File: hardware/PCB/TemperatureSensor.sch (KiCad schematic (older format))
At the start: 14 parts, among them J1 USB_B_Micro, U2 FT230XQ

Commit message: Complete Sensor schematic
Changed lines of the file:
@@
 F0 "Sensor" 50
 F1 "Sensor.sch" 50
+F2 "RST_SHT31" O R 2700 6600 50
+F3 "T_SHT31" O R 2700 6700 50
+F4 "RH_SHT31" O R 2700 6800 50
+F5 "SDA" O R 2700 7050 50
+F6 "SCL" O R 2700 7150 50
 $EndSheet
 $Sheet

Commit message: add 10k pull up
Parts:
- H1, H2, H3, H4: footprint MountingHole:MountingHole_2.2mm_M2_Pad_Via -> MountingHole:MountingHole_3.2mm_M3_Pad_Via
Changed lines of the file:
@@
 F 0 "H1" H 1000 2799 50  0000 L CNN
 F 1 "MountingHole_Pad" H 1000 2708 50  0000 L CNN
-F 2 "MountingHole:MountingHole_2.2mm_M2_Pad_Via" H 900 2750 50  0001 C CNN
+F 2 "MountingHole:MountingHole_3.2mm_M3_Pad_Via" H 900 2750 50  0001 C CNN
 F 3 "~" H 900 2750 50  0001 C CNN
 	1    900  2750
@@
 F 0 "H2" H 2000 2799 50  0000 L CNN
 F 1 "MountingHole_Pad" H 2000 2708 50  0000 L CNN
-F 2 "MountingHole:MountingHole_2.2mm_M2_Pad_Via" H 1900 2750 50  0001 C CNN
+F 2 "MountingHole:MountingHole_3.2mm_M3_Pad_Via" H 1900 2750 50  0001 C CNN
 F 3 "~" H 1900 2750 50  0001 C CNN
 	1    1900 2750
@@
 F 0 "H4" H 1800 3107 50  0000 R CNN
 F 1 "MountingHole_Pad" H 1800 3198 50  0000 R CNN
-F 2 "MountingHole:MountingHole_2.2mm_M2_Pad_Via" H 1900 3150 50  0001 C CNN
+F 2 "MountingHole:MountingHole_3.2mm_M3_Pad_Via" H 1900 3150 50  0001 C CNN
 F 3 "~" H 1900 3150 50  0001 C CNN
 	1    1900 3150
@@
 F 0 "H3" H 800 3107 50  0000 R CNN
 F 1 "MountingHole_Pad" H 800 3198 50  0000 R CNN
-F 2 "MountingHole:MountingHole_2.2mm_M2_Pad_Via" H 900 3150 50  0001 C CNN
+F 2 "MountingHole:MountingHole_3.2mm_M3_Pad_Via" H 900 3150 50  0001 C CNN
 F 3 "~" H 900 3150 50  0001 C CNN
 	1    900  3150

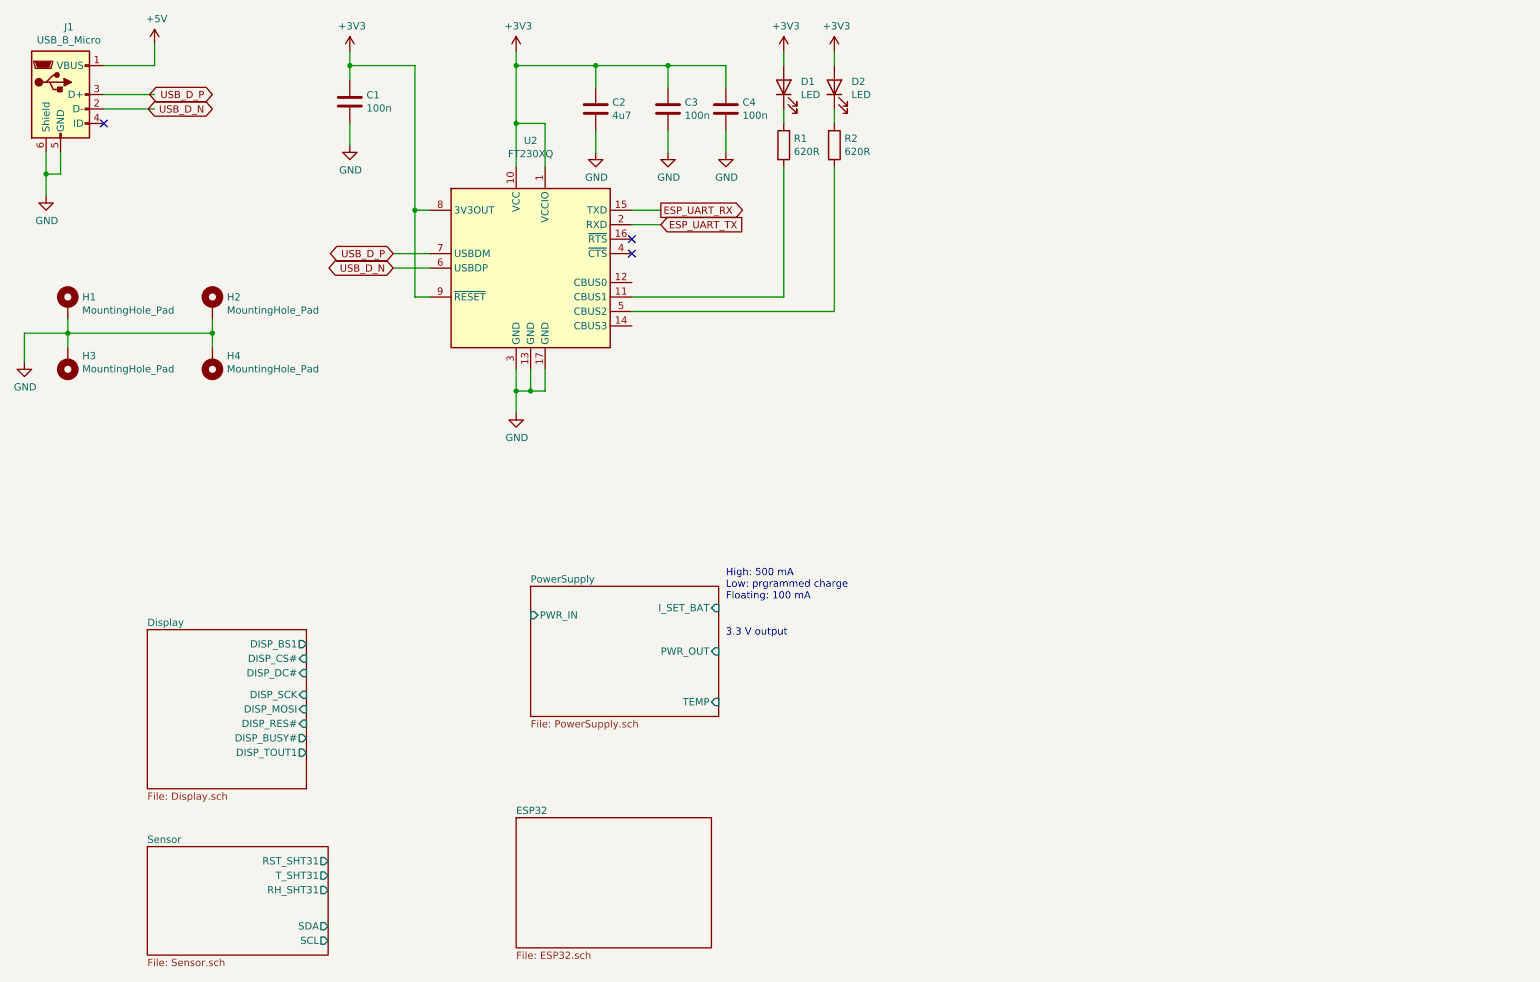
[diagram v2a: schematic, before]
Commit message: add mechannical and usb ftdi sheet
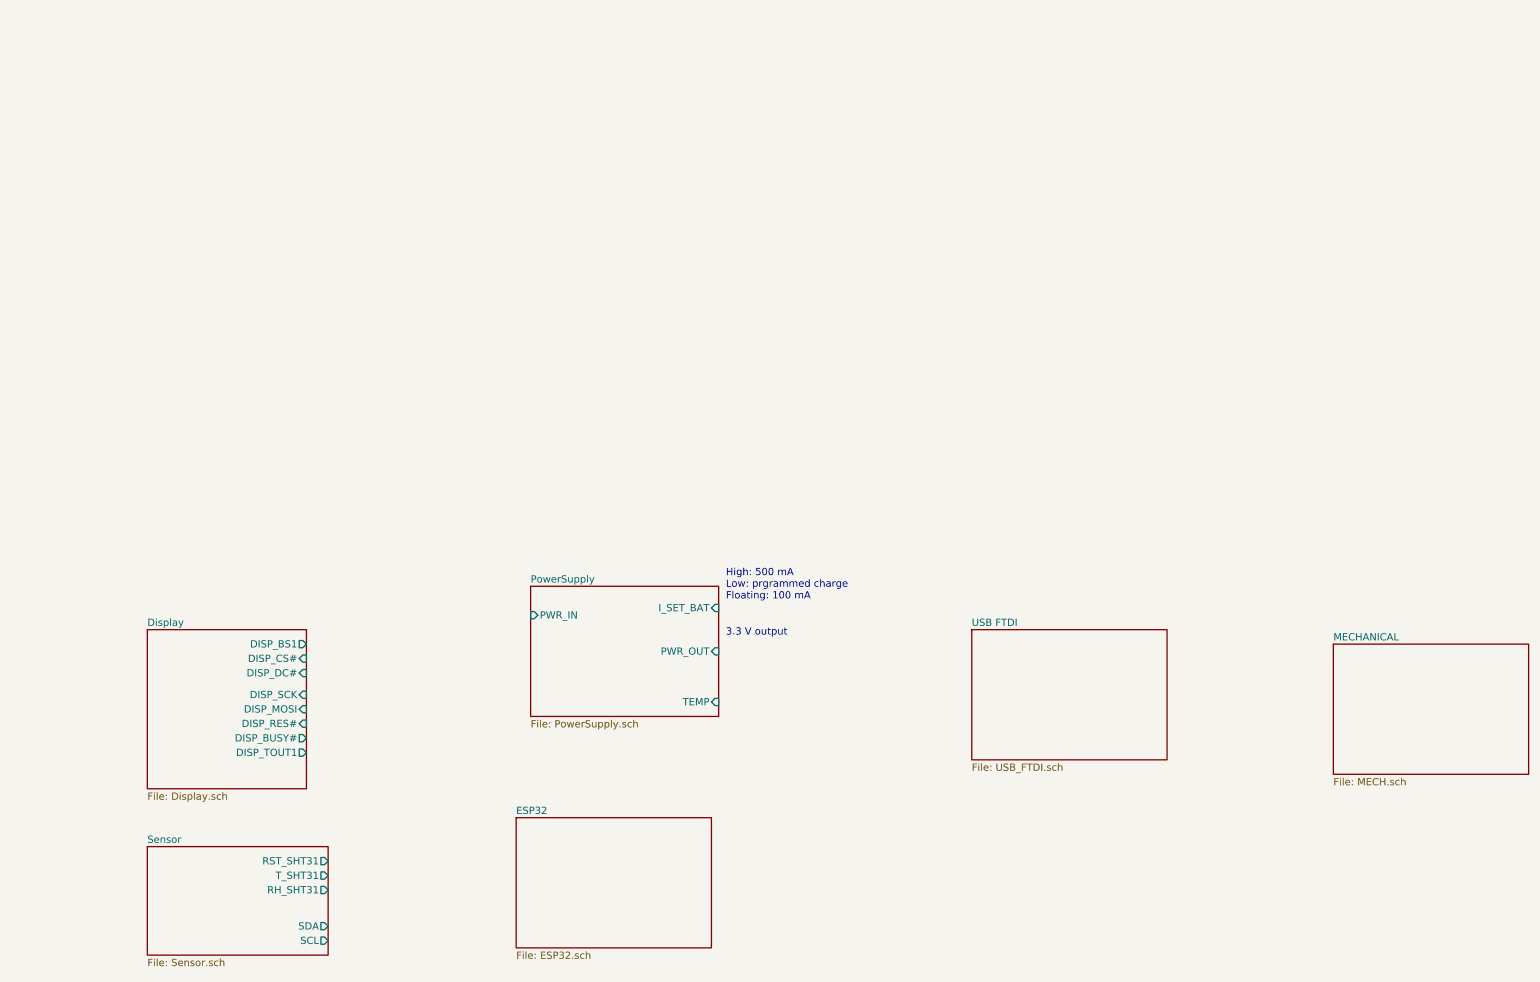
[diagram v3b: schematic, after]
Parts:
- removed C1, C3, C4: 100n, Capacitor_SMD:C_0603_1608Metric, symbol Device:C
- removed C2: 4u7, Capacitor_SMD:C_0603_1608Metric, symbol Device:C
- removed D1, D2: LED, LED_SMD:LED_0603_1608Metric, symbol Device:LED
- removed H1, H2, H3, H4: MountingHole_Pad, MountingHole:MountingHole_3.2mm_M3_Pad_Via, symbol Mechanical:MountingHole_Pad
- removed J1: USB_B_Micro, Connector_USB:USB_Micro-B_Amphenol_10118194_Horizontal, symbol Connector:USB_B_Micro
- removed R1, R2: 620R, Resistor_SMD:R_0603_1608Metric, symbol Device:R
- removed U2: FT230XQ, Package_DFN_QFN:QFN-16-1EP_4x4mm_P0.65mm_EP2.1x2.1mm, symbol Interface_USB:FT230XQ
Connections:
- net labels removed: +3V3, +5V, ESP_UART_RX, ESP_UART_TX, GND, USB_D_N, USB_D_P
- wire segments 55 -> 0
- no-connect marks 3 -> 0

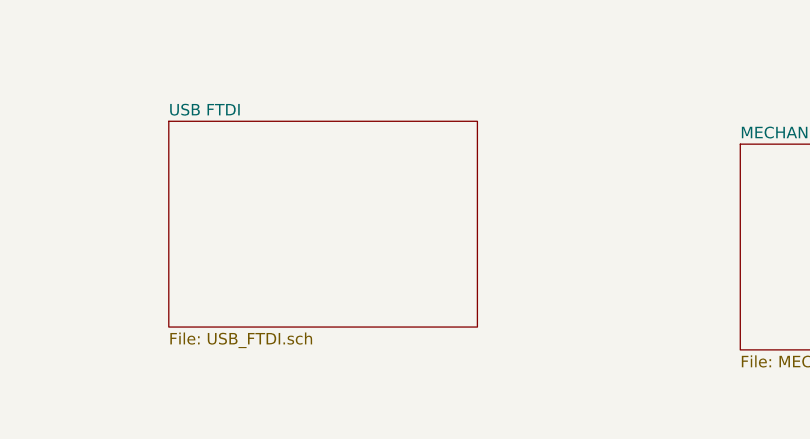
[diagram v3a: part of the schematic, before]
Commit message: add 32khz crystal for rtc
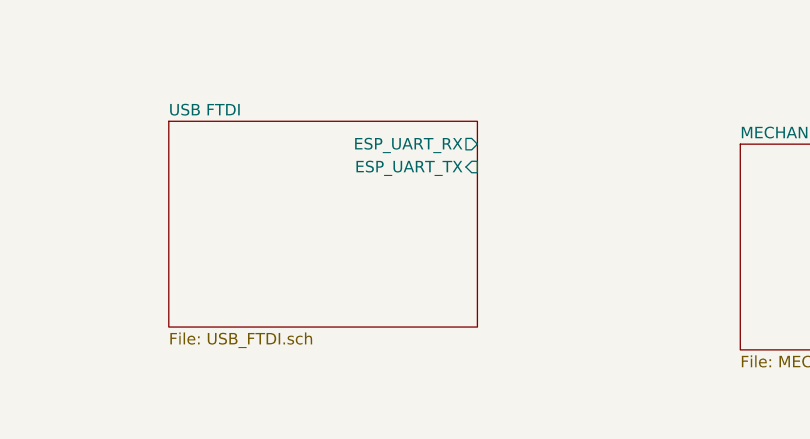
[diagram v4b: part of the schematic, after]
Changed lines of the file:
@@
 F0 "USB FTDI" 50
 F1 "USB_FTDI.sch" 50
+F2 "ESP_UART_RX" O R 8500 5100 50
+F3 "ESP_UART_TX" I R 8500 5200 50
 $EndSheet
 $EndSCHEMATC

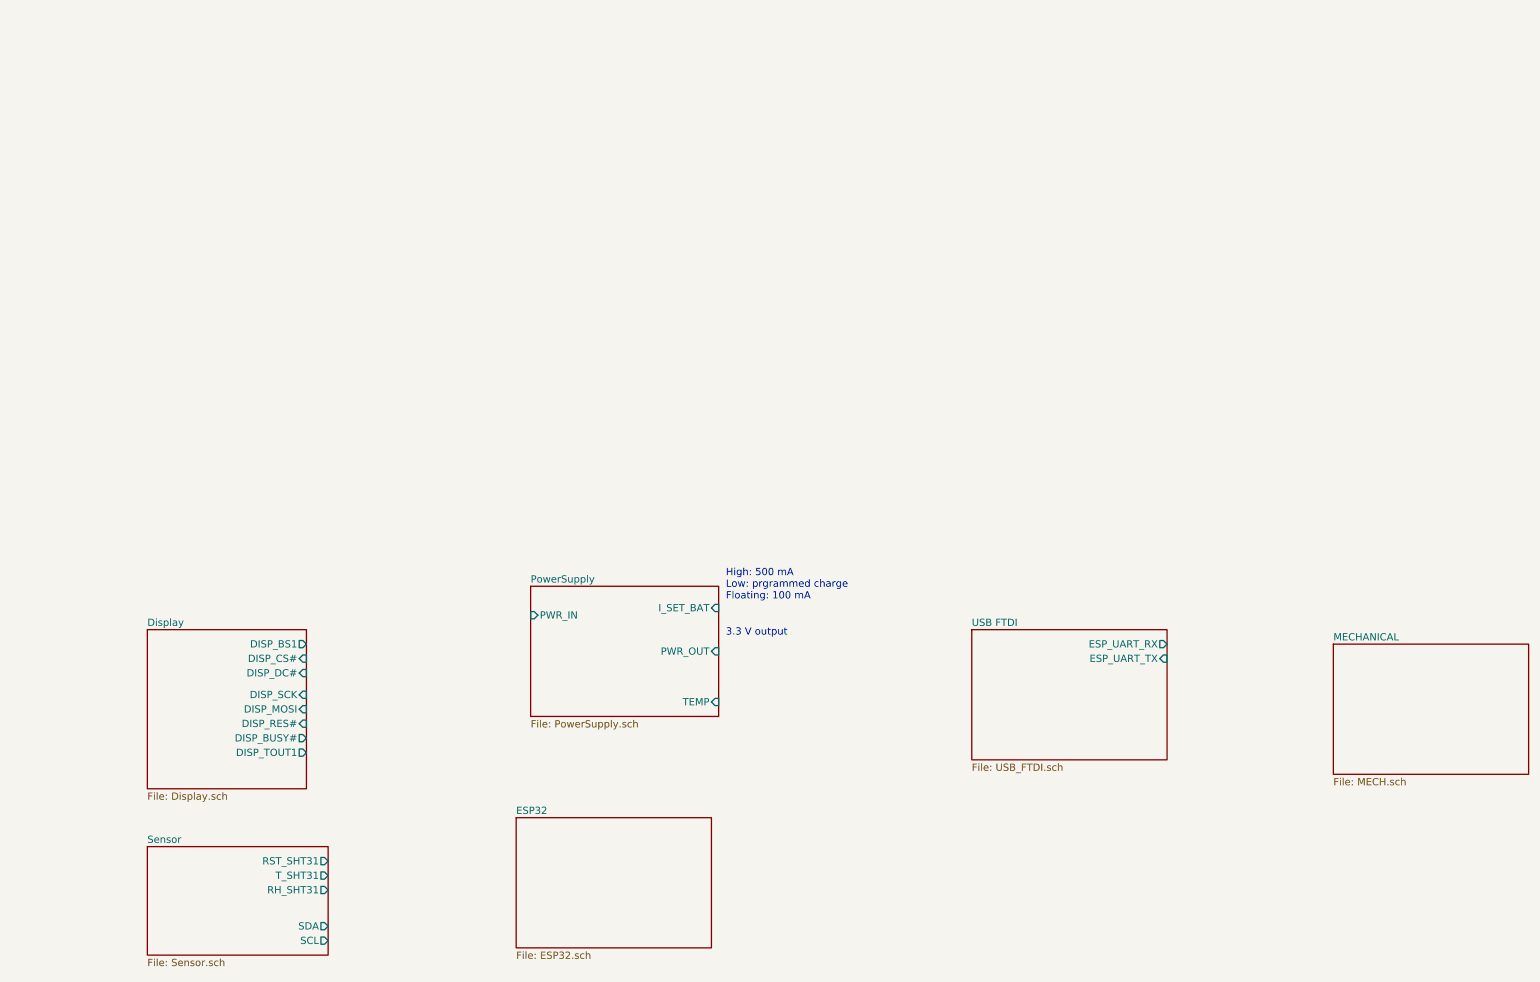
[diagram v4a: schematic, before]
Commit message: corrected power supply schematic
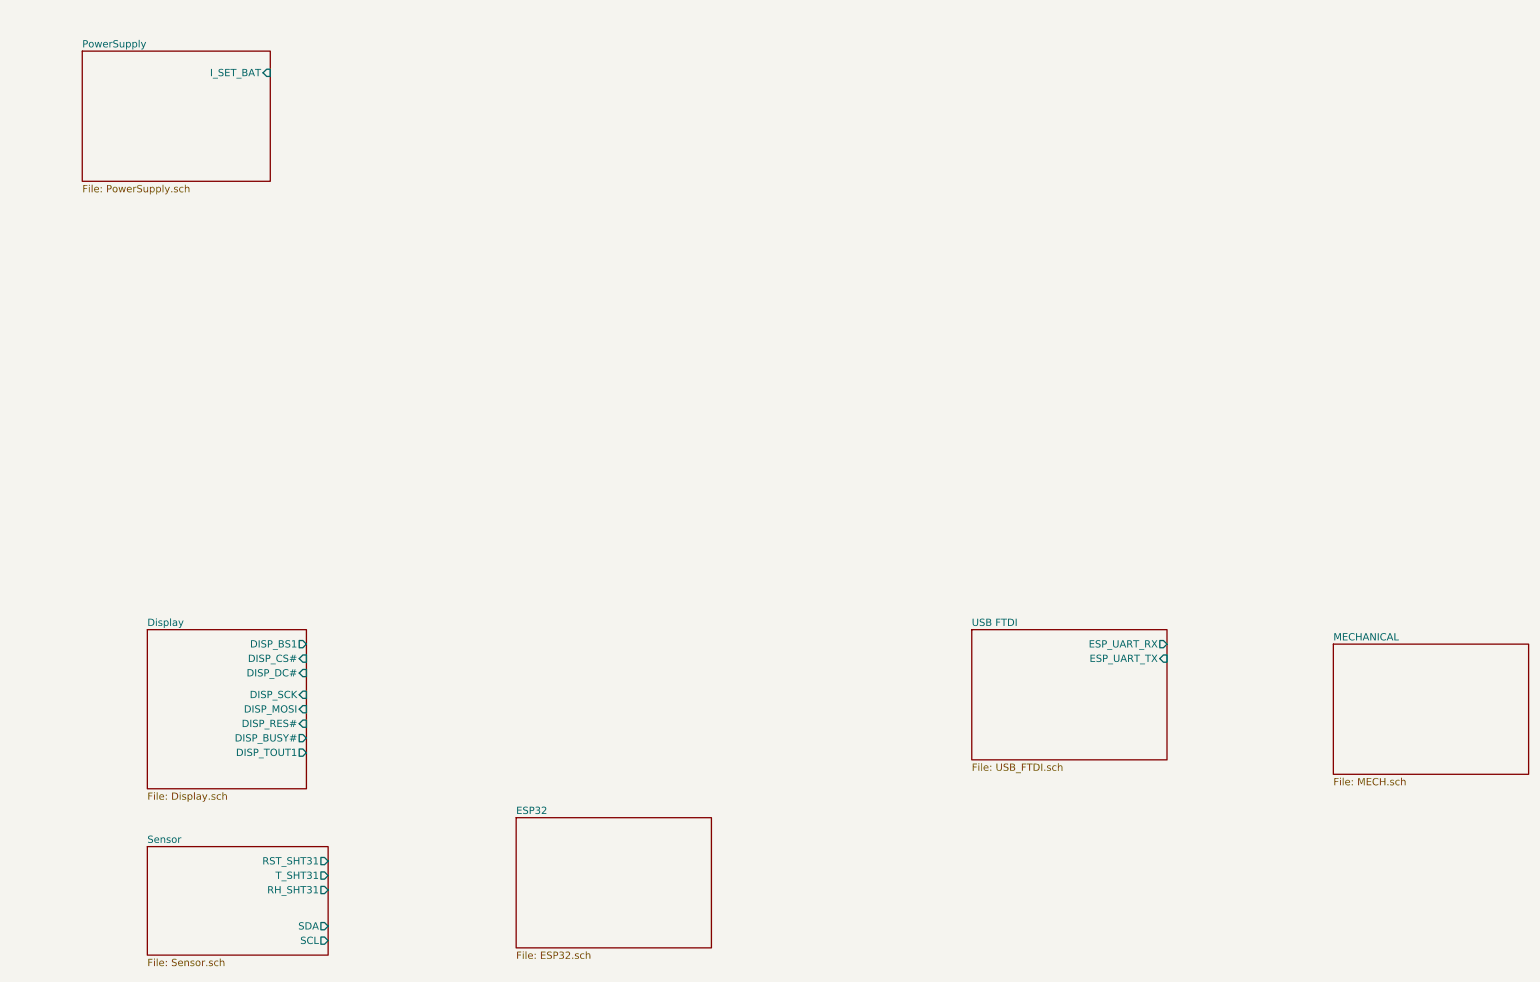
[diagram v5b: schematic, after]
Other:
- note removed: "3.3 V output"
- note removed: "High: 500 mA\nLow: prgrammed charge\nFloating: 100 mA"
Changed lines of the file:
@@
 $EndDescr
 $Sheet
-S 4100 4700 1300 900
+S 1000 1000 1300 900
 U 5FBFD530
 F0 "PowerSupply" 50
 F1 "PowerSupply.sch" 50
-F2 "PWR_IN" I L 4100 4900 50
-F3 "I_SET_BAT" I R 5400 4850 50
-F4 "TEMP" I R 5400 5500 50
-F5 "PWR_OUT" I R 5400 5150 50
+F2 "I_SET_BAT" I R 2300 1150 50
 $EndSheet
-Text Notes 5450 4800 0    50   ~ 0
-High: 500 mA\nLow: prgrammed charge\nFloating: 100 mA
-Text Notes 5450 5050 0    50   ~ 0
-3.3 V output
 $Sheet
 S 1450 5000 1100 1100

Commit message: add 40 MHz crystal
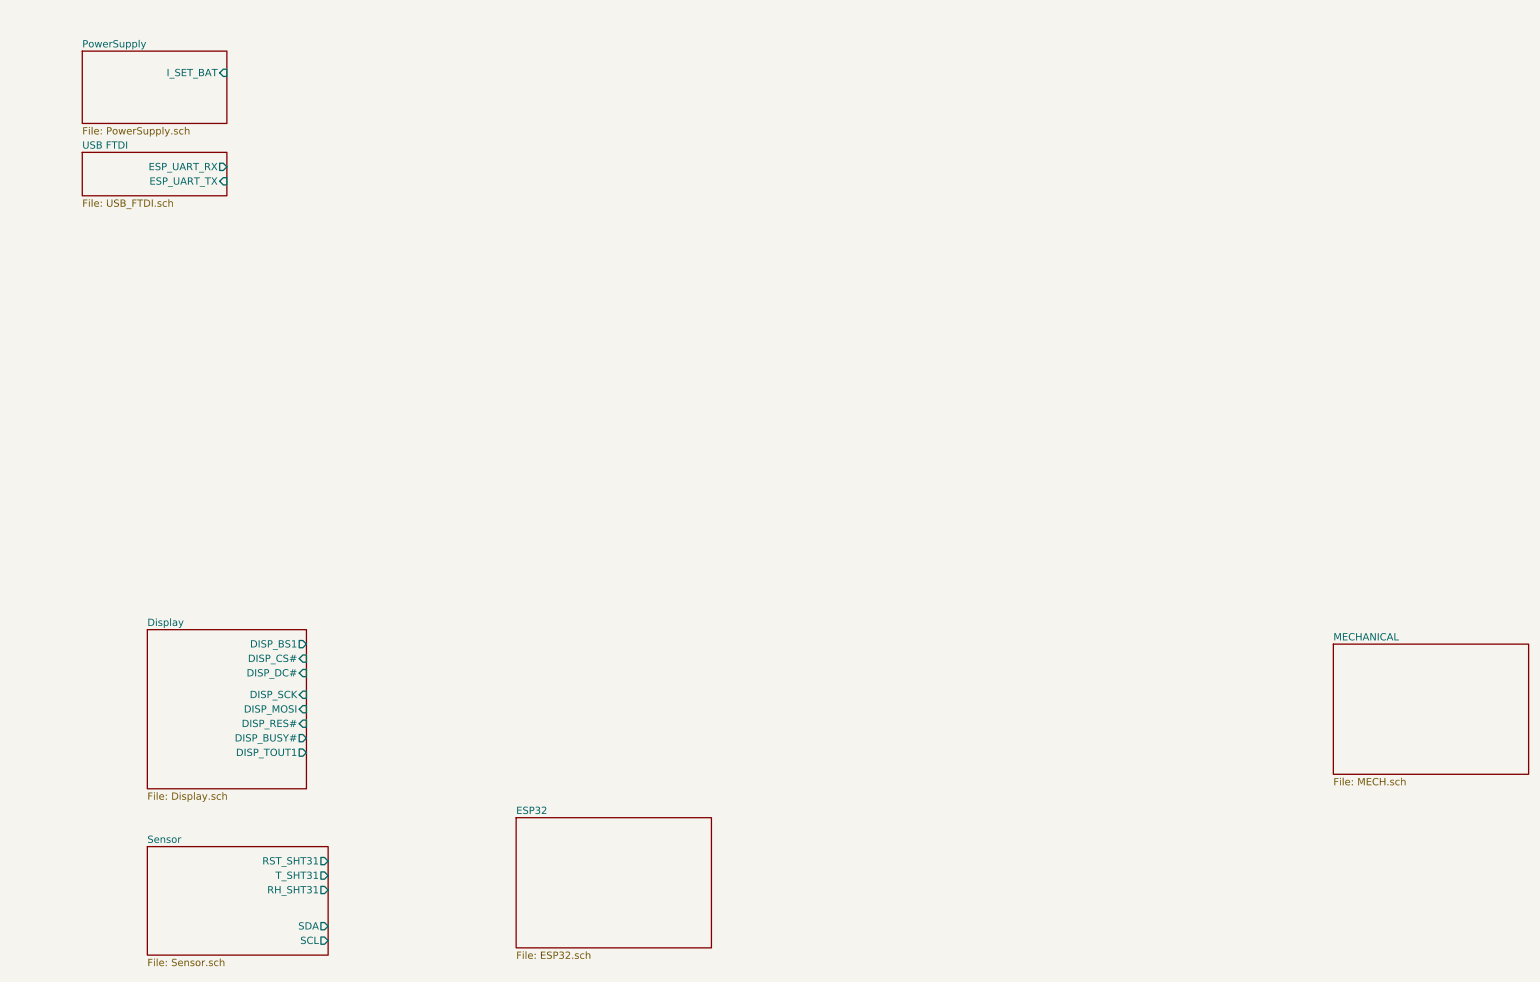
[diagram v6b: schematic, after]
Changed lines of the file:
@@
 $EndDescr
 $Sheet
-S 1000 1000 1300 900
+S 1000 1000 1000 500
 U 5FBFD530
 F0 "PowerSupply" 50
 F1 "PowerSupply.sch" 50
-F2 "I_SET_BAT" I R 2300 1150 50
+F2 "I_SET_BAT" I R 2000 1150 50
 $EndSheet
 $Sheet
@@
 $EndSheet
 $Sheet
-S 7150 5000 1350 900
+S 1000 1700 1000 300
 U 5FE9624E
 F0 "USB FTDI" 50
 F1 "USB_FTDI.sch" 50
-F2 "ESP_UART_RX" O R 8500 5100 50
-F3 "ESP_UART_TX" I R 8500 5200 50
+F2 "ESP_UART_RX" O R 2000 1800 50
+F3 "ESP_UART_TX" I R 2000 1900 50
 $EndSheet
 $EndSCHEMATC
